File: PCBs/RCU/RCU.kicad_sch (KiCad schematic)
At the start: 0 parts

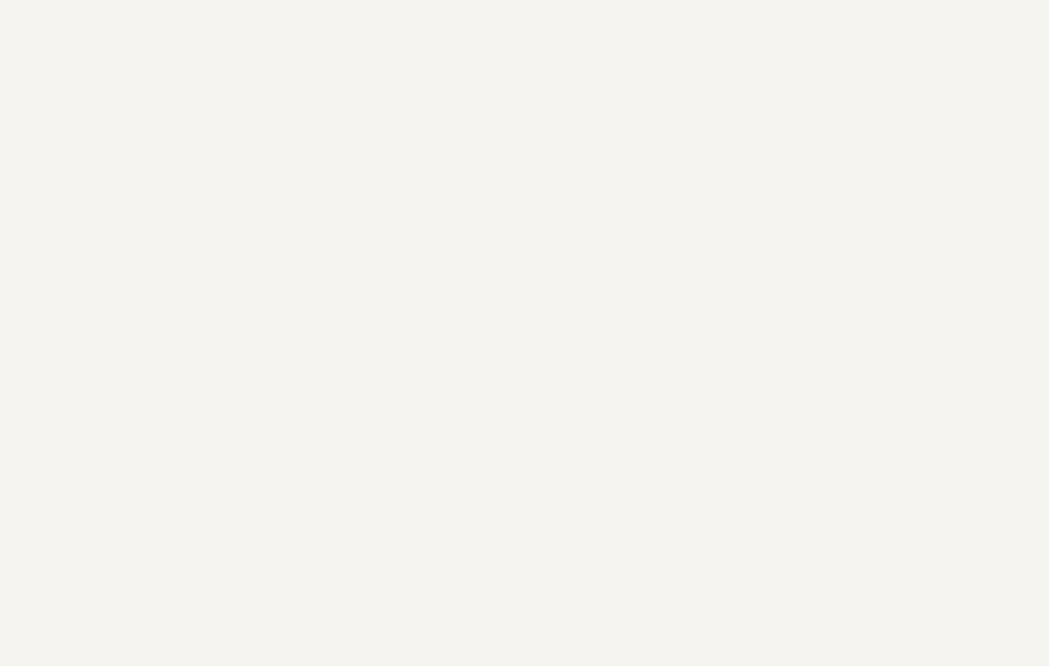
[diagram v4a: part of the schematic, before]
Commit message: Added 32Mbit external memory with SPI interface
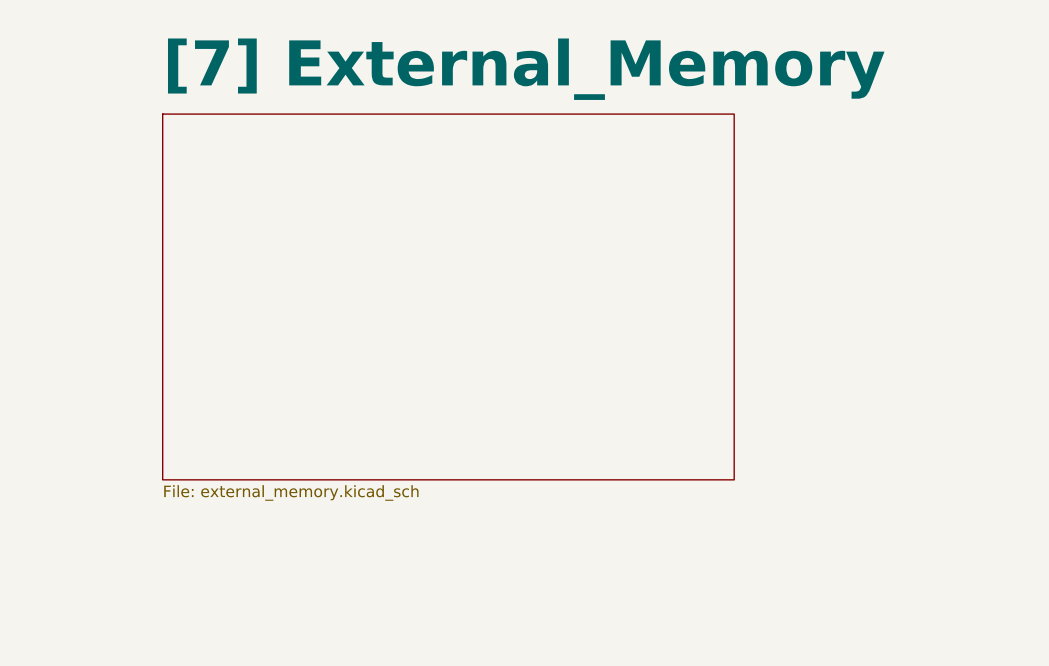
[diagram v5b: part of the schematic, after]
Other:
- added sheet [7] External_Memory (external_memory.kicad_sch)
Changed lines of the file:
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@@
+    )
+  )
+  (sheet (at 182.88 26.67) (size 63.5 40.64) (fields_autoplaced)
+    (stroke (width 0.1524) (type solid) (color 0 0 0 0))
+    (fill (color 0 0 0 0.0000))
+    (property "Sheet name" "[7] External_Memory" (id 0) (at 182.88 24.0934 0)
+      (effects (font (size 5 5) bold) (justify left bottom))
+    )
+    (property "Sheet file" "external_memory.kicad_sch" (id 1) (at 182.88 67.8946 0)
+      (effects (font (size 1.27 1.27)) (justify left top))
     )
   )
@@
     (path "/2af55460-e33d-4dc0-b588-5a5fc90e3fb4" (page "6"))
     (path "/b265f195-de32-404f-a73c-b2d5ee499e9b" (page "7"))
+    (path "/30f70446-f8fc-40ff-92fb-56eae08fade9" (page "8"))
   )
   (symbol_instances
@@
       (reference "#PWR?") (unit 1) (value "+3.3VA") (footprint "")
     )
+    (path "/30f70446-f8fc-40ff-92fb-56eae08fade9/2c4a4823-3df4-4715-82e4-ace04f59e52b"
+      (reference "#PWR?") (unit 1) (value "+3.3V") (footprint "")
+    )
     (path "/2af55460-e33d-4dc0-b588-5a5fc90e3fb4/2c9c7684-021c-41cf-9d0d-1fa35382c302"
       (reference "#PWR?") (unit 1) (value "GND") (footprint "")
@@
       (reference "#PWR?") (unit 1) (value "GND") (footprint "")
     )
+    (path "/30f70446-f8fc-40ff-92fb-56eae08fade9/a3d05544-1aaa-4025-afbf-bfda71669845"
+      (reference "#PWR?") (unit 1) (value "GND") (footprint "")
+    )
     (path "/d249f484-be7b-4fe1-aa74-bf5965c8a2c2/a8c64bdd-4bad-4dfe-9947-e954dc30b04b"
       (reference "#PWR?") (unit 1) (value "+3.3VA") (footprint "")
@@
       (reference "C605") (unit 1) (value "0.1u") (footprint "")
     )
+    (path "/30f70446-f8fc-40ff-92fb-56eae08fade9/7de61893-ae1e-4617-b417-e465acfee189"
+      (reference "C?") (unit 1) (value "1uF") (footprint "")
+    )
     (path "/b265f195-de32-404f-a73c-b2d5ee499e9b/8a888a78-4b14-4632-9ecc-d31e8c291f42"
       (reference "D100") (unit 1) (value "SM5817") (footprint "")
@@
       (reference "U603") (unit 1) (value "OPA365xxD") (footprint "Package_SO:SOIC-8_3.9x4.9mm_P1.27mm")
     )
+    (path "/30f70446-f8fc-40ff-92fb-56eae08fade9/d9d8767a-f1c1-4f00-b775-6d4cbe435572"
+      (reference "U?") (unit 1) (value "SST26VF032BT-104I/SM") (footprint "Package_SO:SOIC-8_5.275x5.275mm_P1.27mm")
+    )
     (path "/c46a482e-bfa4-4ed5-a49f-3179709c39a1/29eeaf52-5c5c-474e-9bf9-93b8570a7d73"
